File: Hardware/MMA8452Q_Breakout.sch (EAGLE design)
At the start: 16 parts, among them U1 MMA8452QMMA8452Q-1:1

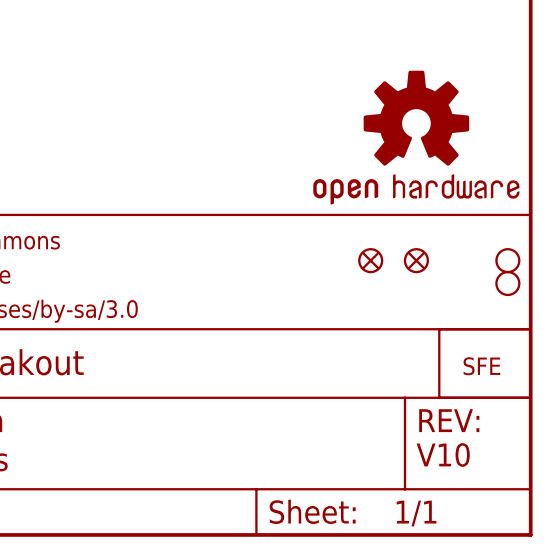
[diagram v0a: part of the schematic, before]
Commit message: added board fiducials
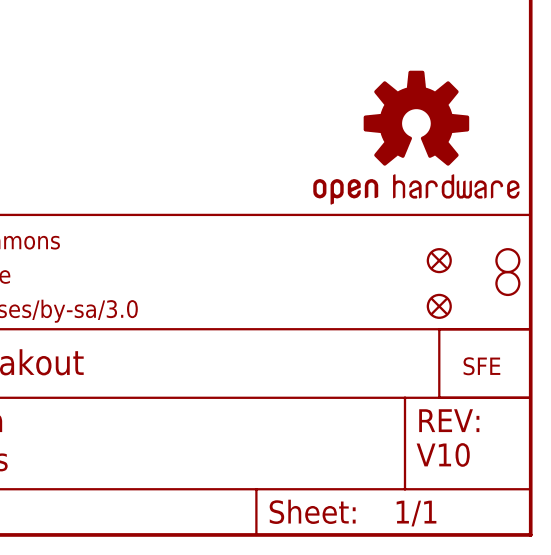
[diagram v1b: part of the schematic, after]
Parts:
- removed JP2, JP6: FIDUCIALUFIDUCIAL, SparkFun:FIDUCIALUFIDUCIAL
- added FID1, FID2: FIDUCIAL1X2, SparkFun-Aesthetics:FIDUCIAL1X2
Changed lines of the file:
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@@
 <?xml version="1.0" encoding="utf-8"?>
 <!DOCTYPE eagle SYSTEM "eagle.dtd">
-<eagle version="6.4">
+<eagle version="6.5.0">
 <drawing>
 <settings>
@@
 <part name="JP5" library="SparkFun" deviceset="M06" device="SIP"/>
 <part name="SJ1" library="SparkFun" deviceset="SOLDERJUMPER" device="NO" value=""/>
-<part name="JP2" library="SparkFun" deviceset="FIDUCIAL" device="UFIDUCIAL"/>
-<part name="JP6" library="SparkFun" deviceset="FIDUCIAL" device="UFIDUCIAL"/>
+<part name="FID1" library="SparkFun-Aesthetics" deviceset="FIDUCIAL" device="1X2"/>
+<part name="FID2" library="SparkFun-Aesthetics" deviceset="FIDUCIAL" device="1X2"/>
 </parts>
 <sheets>
@@
 <instance part="JP5" gate="G$1" x="193.04" y="101.6" rot="R180"/>
 <instance part="SJ1" gate="1" x="162.56" y="83.82" rot="R90"/>
-<instance part="JP2" gate="G$1" x="231.14" y="30.48"/>
-<instance part="JP6" gate="G$1" x="236.22" y="30.48"/>
+<instance part="FID1" gate="G$1" x="238.76" y="30.48"/>
+<instance part="FID2" gate="G$1" x="238.76" y="25.4"/>
 </instances>
 <busses>
